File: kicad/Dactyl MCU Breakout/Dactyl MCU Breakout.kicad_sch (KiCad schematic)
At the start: 12 parts

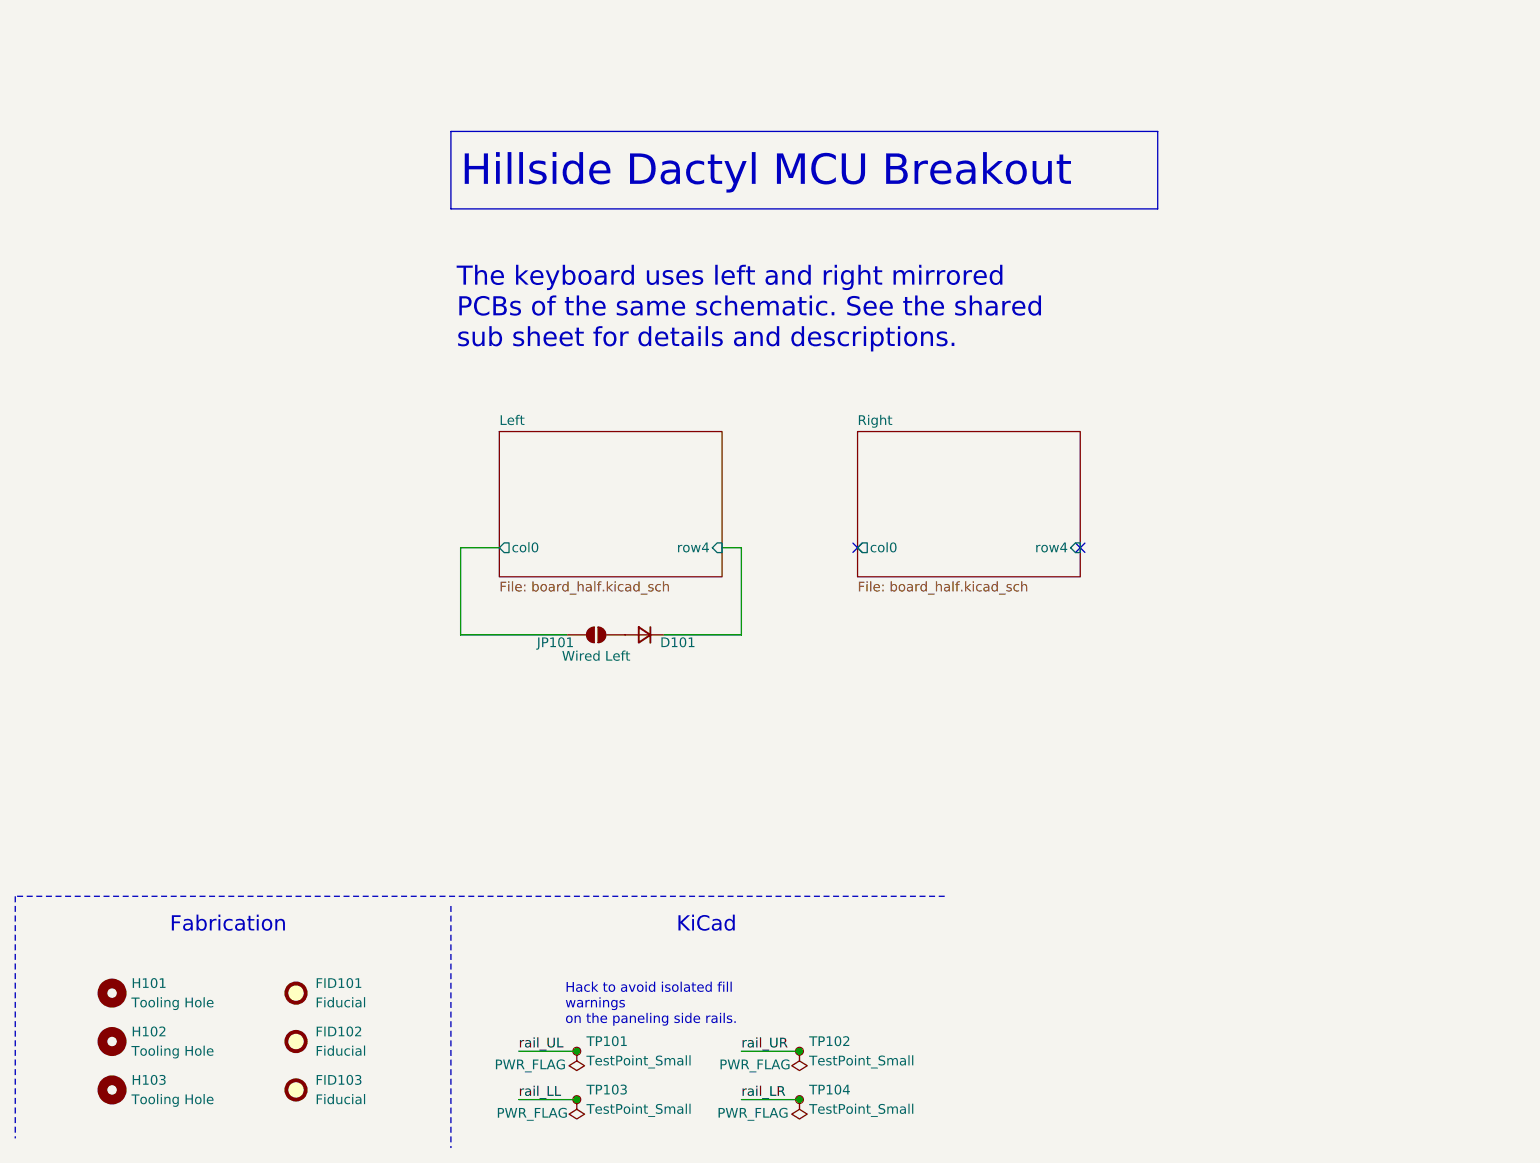
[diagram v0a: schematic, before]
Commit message: feat: split two wire crossed TX/RX UART
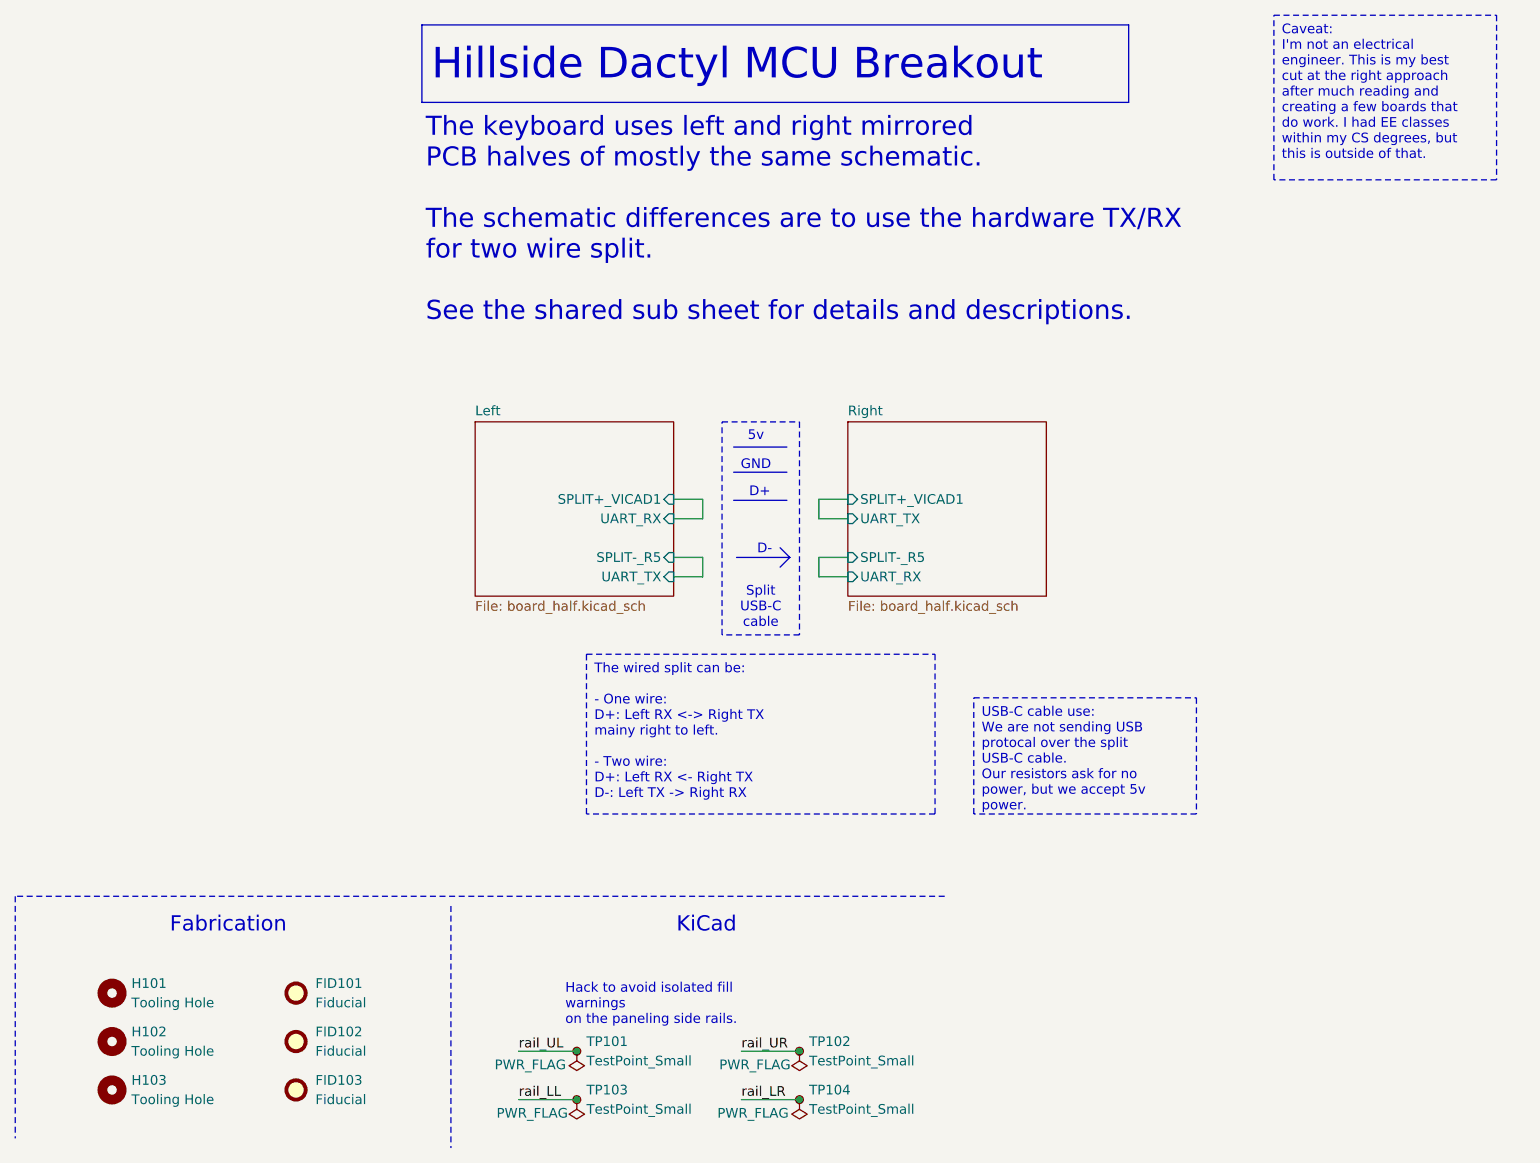
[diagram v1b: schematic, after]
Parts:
- removed D101: D_Small, Diode_SMD:D_SOD-323, symbol Device:D_Small
- removed JP101: Wired Left, Dactyl_basics:SolderJumper-2_P1.3mm_Open_RoundedPad1.0x1.5mm, symbol Jumper:SolderJumper_2_Open
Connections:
- no-connect marks 2 -> 0
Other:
- sheet Left ports: added SPLIT+_VICAD1, SPLIT-_R5, UART_RX, UART_TX; removed col0, row4
- sheet Right ports: added SPLIT+_VICAD1, SPLIT-_R5, UART_RX, UART_TX; removed col0, row4
- note added: "5v"
- note added: "D+"
- note added: "D-"
- note added: "GND"
- note added: "The keyboard uses left and right mirrored PCB halves of mostly the same schematic. The schematic differences are to use the hardware TX/RX for two wire split. See the shared sub sheet for details and descriptions."
- note removed: "The keyboard uses left and right mirrored PCBs of the same schematic. See the shared sub sheet for details and descriptions."
